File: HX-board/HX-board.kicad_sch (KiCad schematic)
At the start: 21 parts, among them J1 Testpoints, J2 PCIE-LP-01-01-F-DV-A-TR, J3 DB15_Female, J4 Testpoints, J5 DB15_Female

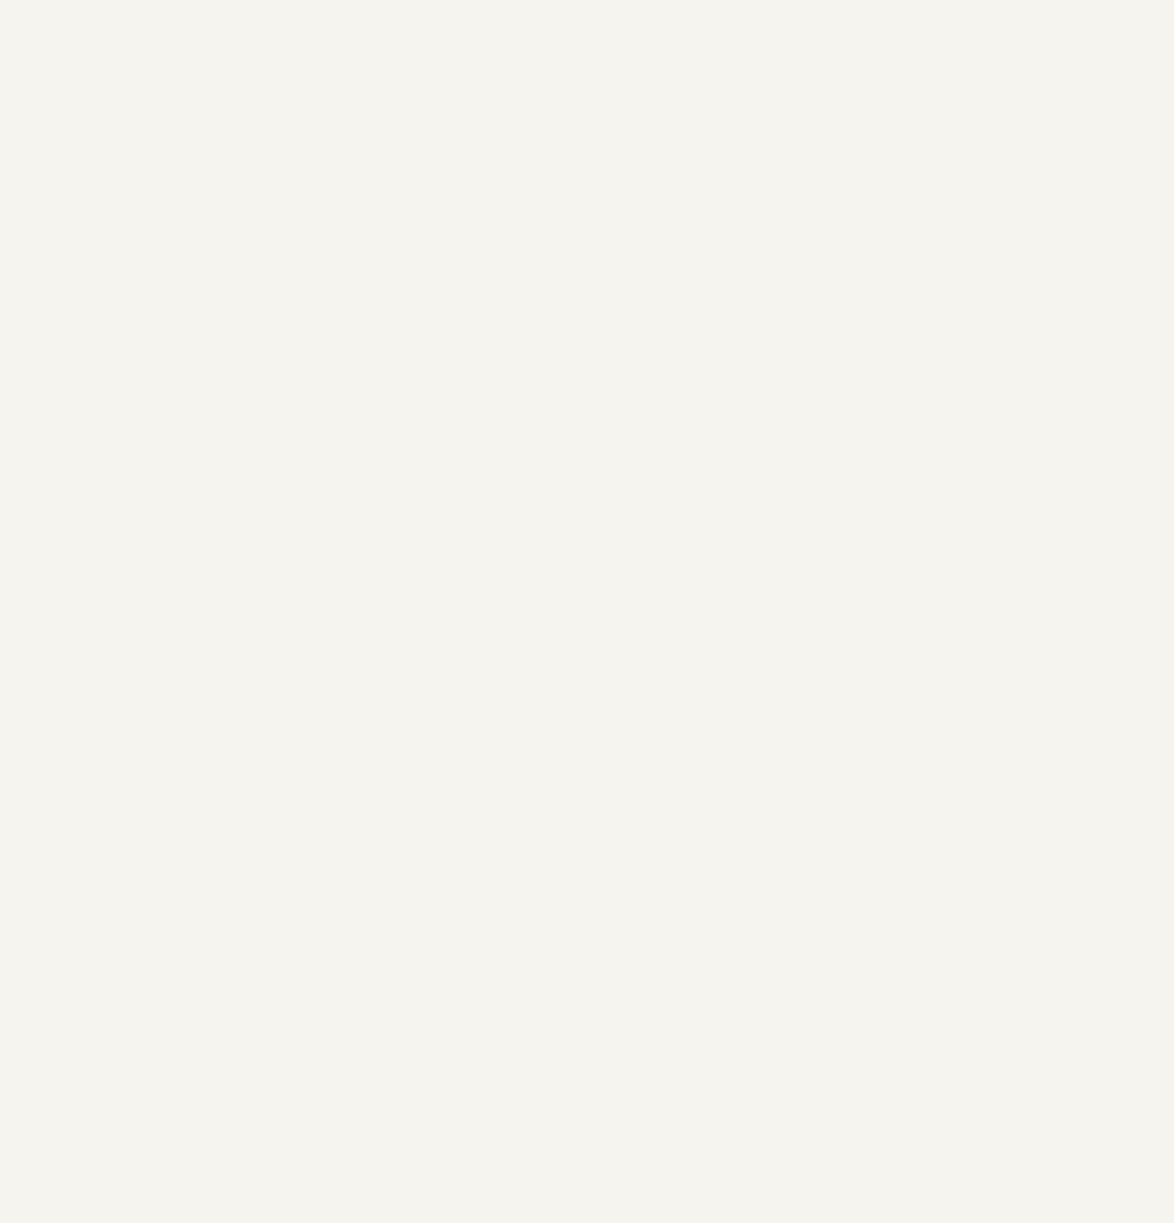
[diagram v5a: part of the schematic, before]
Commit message: Revising PCIe.
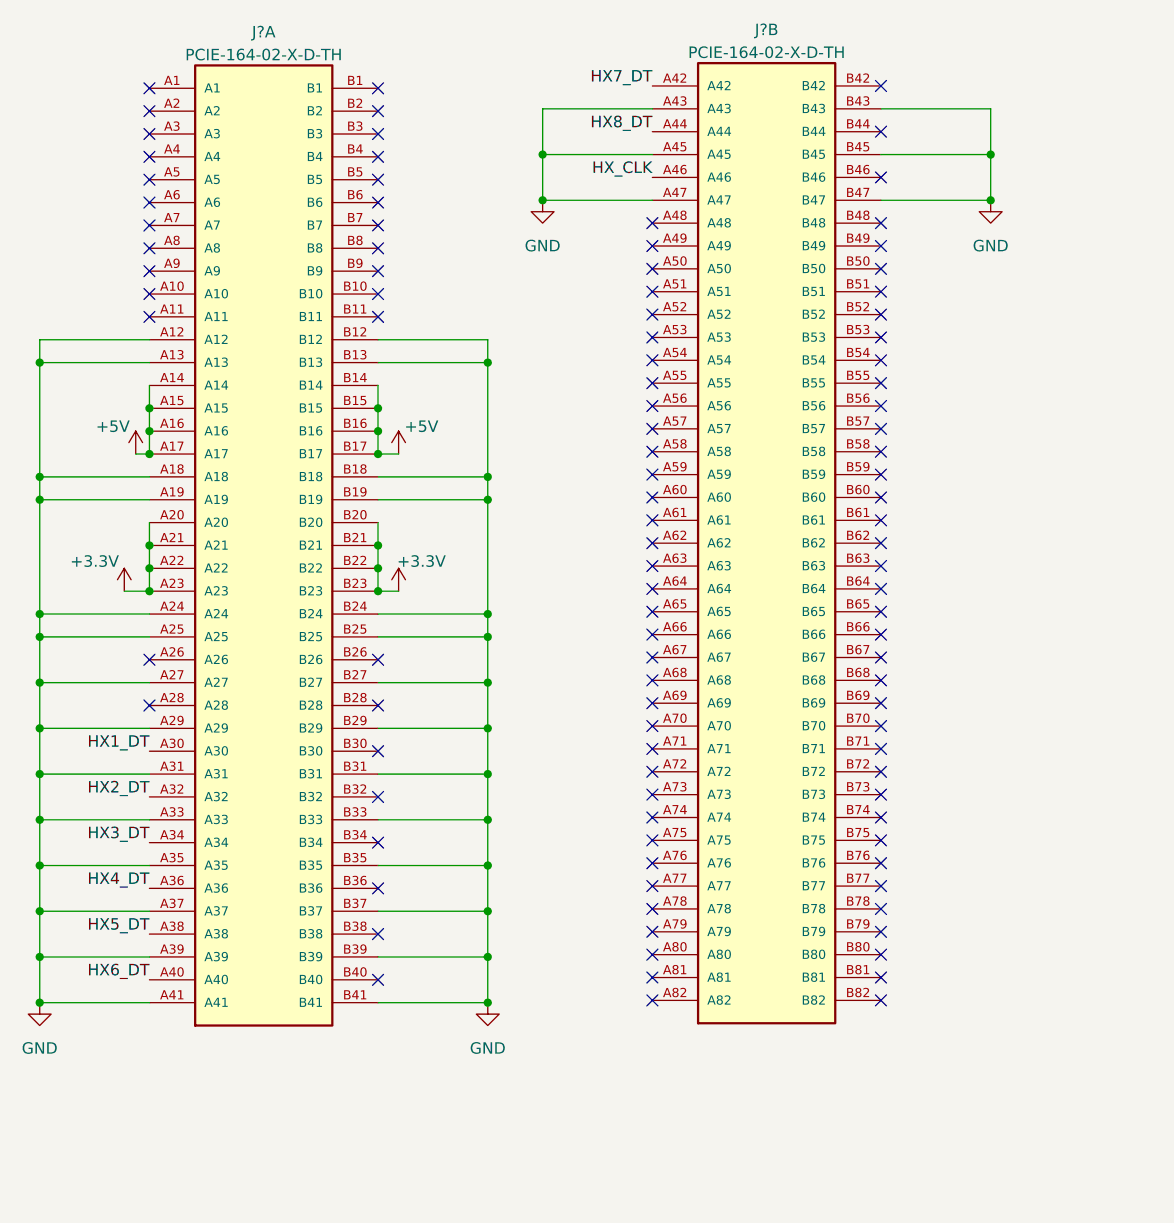
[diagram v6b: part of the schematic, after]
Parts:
- added J? (x2): PCIE-164-02-X-D-TH, PCIE-164-02-X-D-TH:SAMTEC_PCIE-164-02-X-D-TH, symbol PCIE-164-02-X-D-TH:PCIE-164-02-X-D-TH
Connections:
- net +3.3V: now also J?.A20, J?.A21, J?.A22, J?.A23, J?.B20, J?.B21, J?.B22, J?.B23
- net +5V: now also J?.A14, J?.A15, J?.A16, J?.A17, J?.B14, J?.B15, J?.B16, J?.B17
- net GND: now also J?.A12, J?.A13, J?.A18, J?.A19, J?.A24, J?.A25, J?.A27, J?.A29, J?.A31, J?.A33, J?.A35, J?.A37, J?.A39, J?.A41, J?.A43, J?.A45, J?.A47, J?.B12, J?.B13, J?.B18, J?.B19, J?.B24, J?.B25, J?.B27, J?.B29, J?.B31, J?.B33, J?.B35, J?.B37, J?.B39, J?.B41, J?.B43, J?.B45, J?.B47
- net HX1_DT: now also J?.A30
- net HX2_DT: now also J?.A32
- net HX3_DT: now also J?.A34
- net HX4_DT: now also J?.A36
- net HX5_DT: now also J?.A38
- net HX6_DT: now also J?.A40
- net HX7_DT: now also J?.A42
- net HX8_DT: now also J?.A44
- net HX_CLK: now also J?.A46
- no-connect marks 28 -> 133

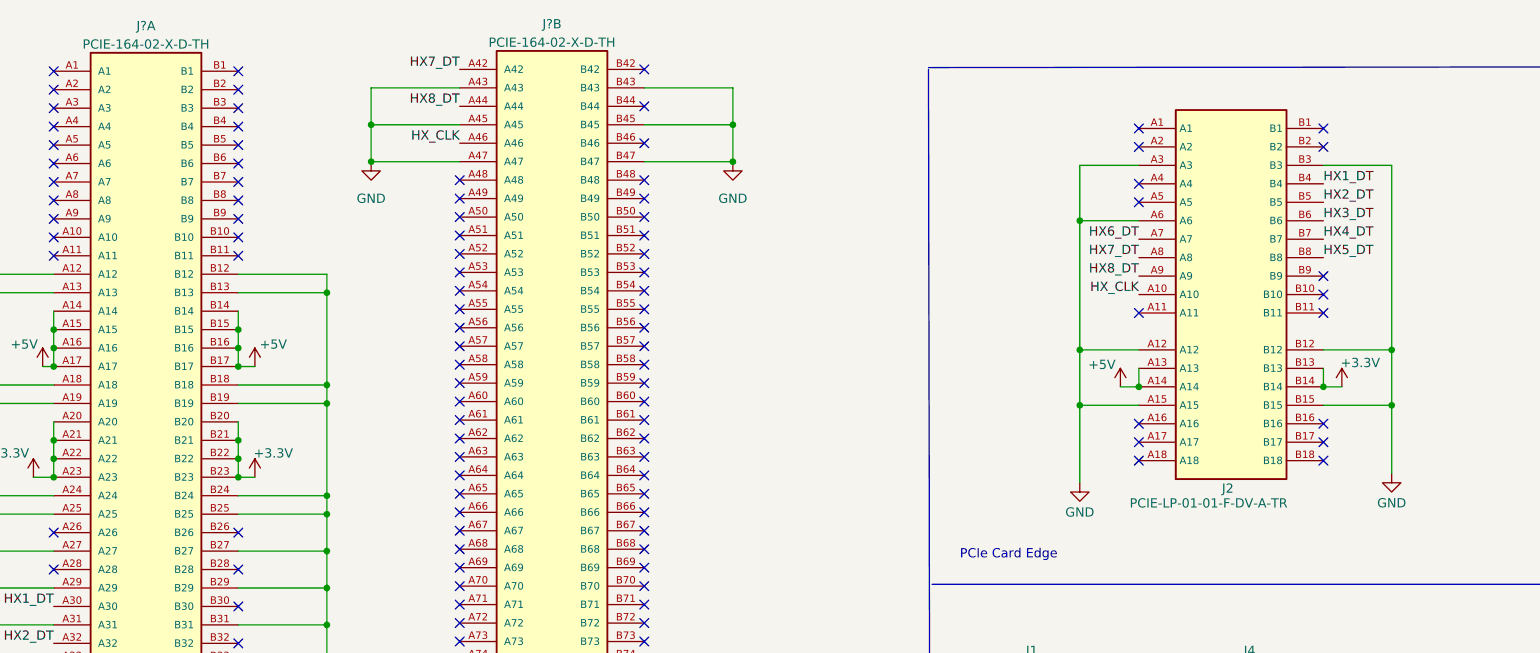
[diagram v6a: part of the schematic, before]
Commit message: Ironing out small details, changed pcf8575 to IC instead of breakout.
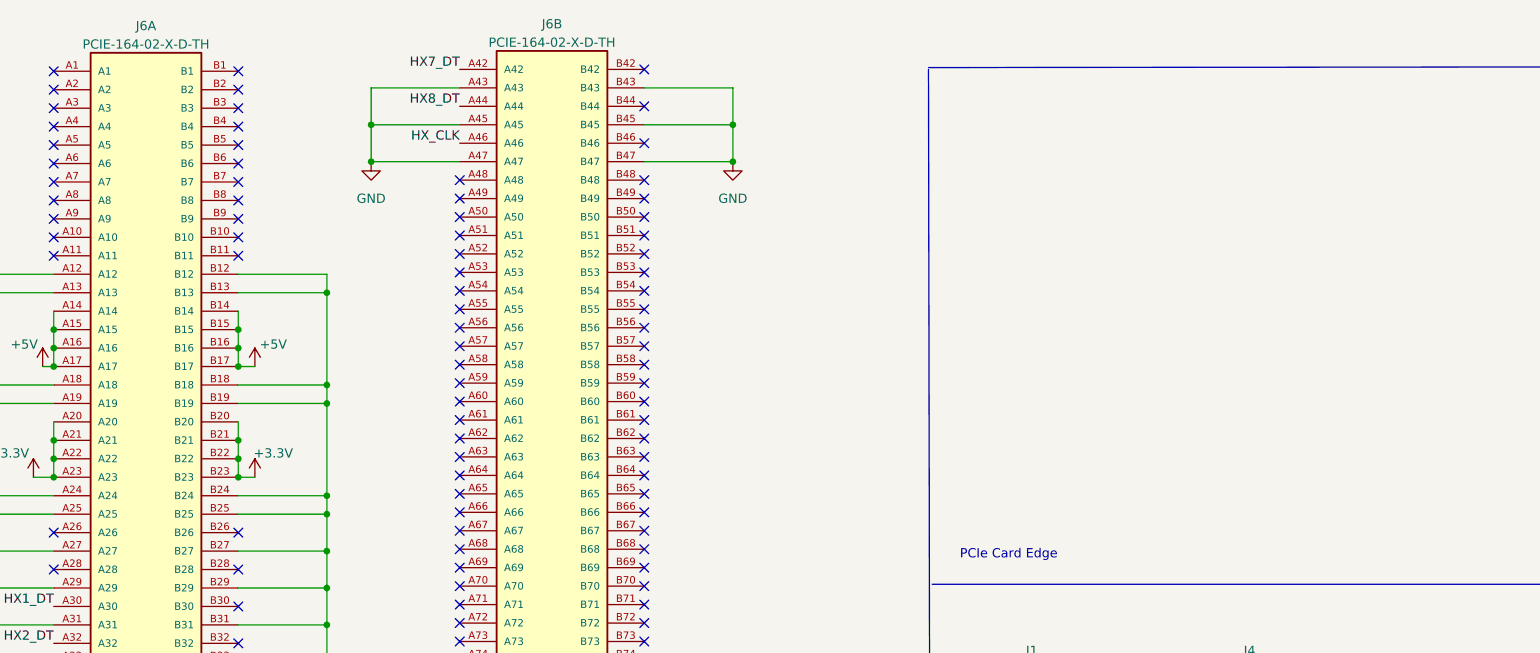
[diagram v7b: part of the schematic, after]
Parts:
- removed J2: PCIE-LP-01-01-F-DV-A-TR, Connector_PCBEdge:BUS_PCIexpress_x1, symbol PCIE_Card_Edge:PCIE-LP-01-01-F-DV-A-TR_(card_edge)
- gave numbers to parts that had none: 1
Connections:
- no-connect marks 133 -> 117
